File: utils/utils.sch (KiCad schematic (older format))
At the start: 37 parts, among them J1 AIN, J2 BIN, J3 GATE, J4 EURORACK_CONN_10, J5 ~OUT, J6 OUT, J7 Conn_01x04, J8 Conn_01x05, J9 Conn_01x03_Male, Q1 2N3904, U1 TL072, U2 4066, U3 LM317L_TO92, U4 LM337_SOT223

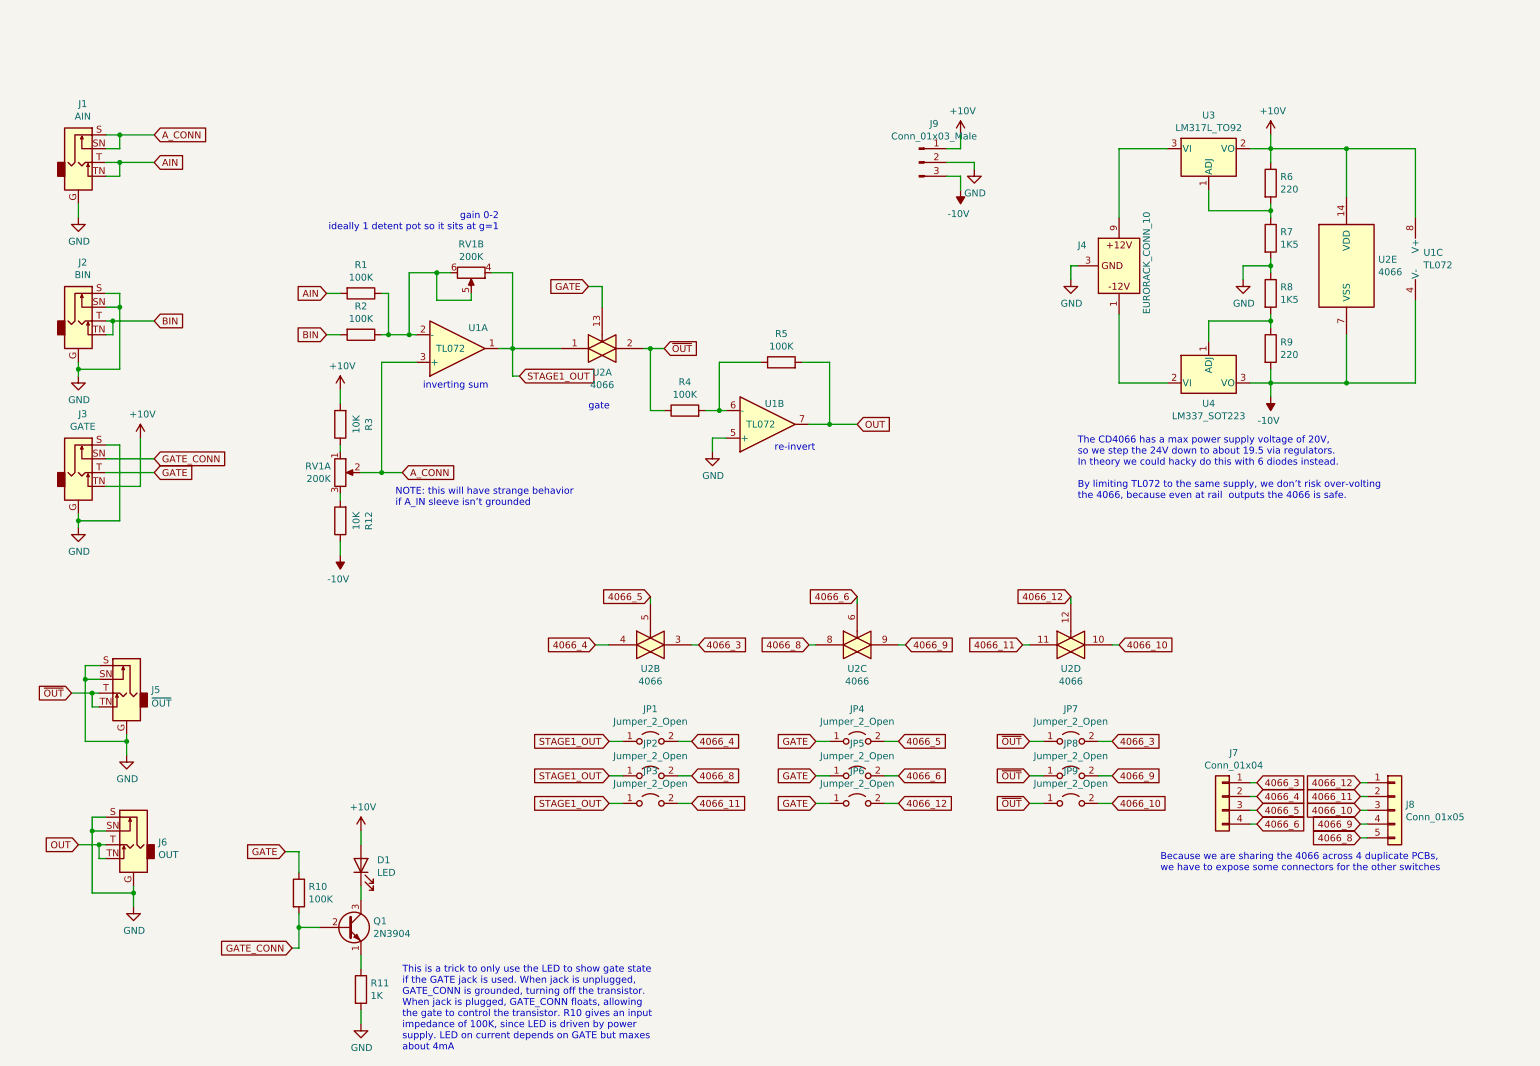
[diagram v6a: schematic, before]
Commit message: reworked utilities around better analog switch modules
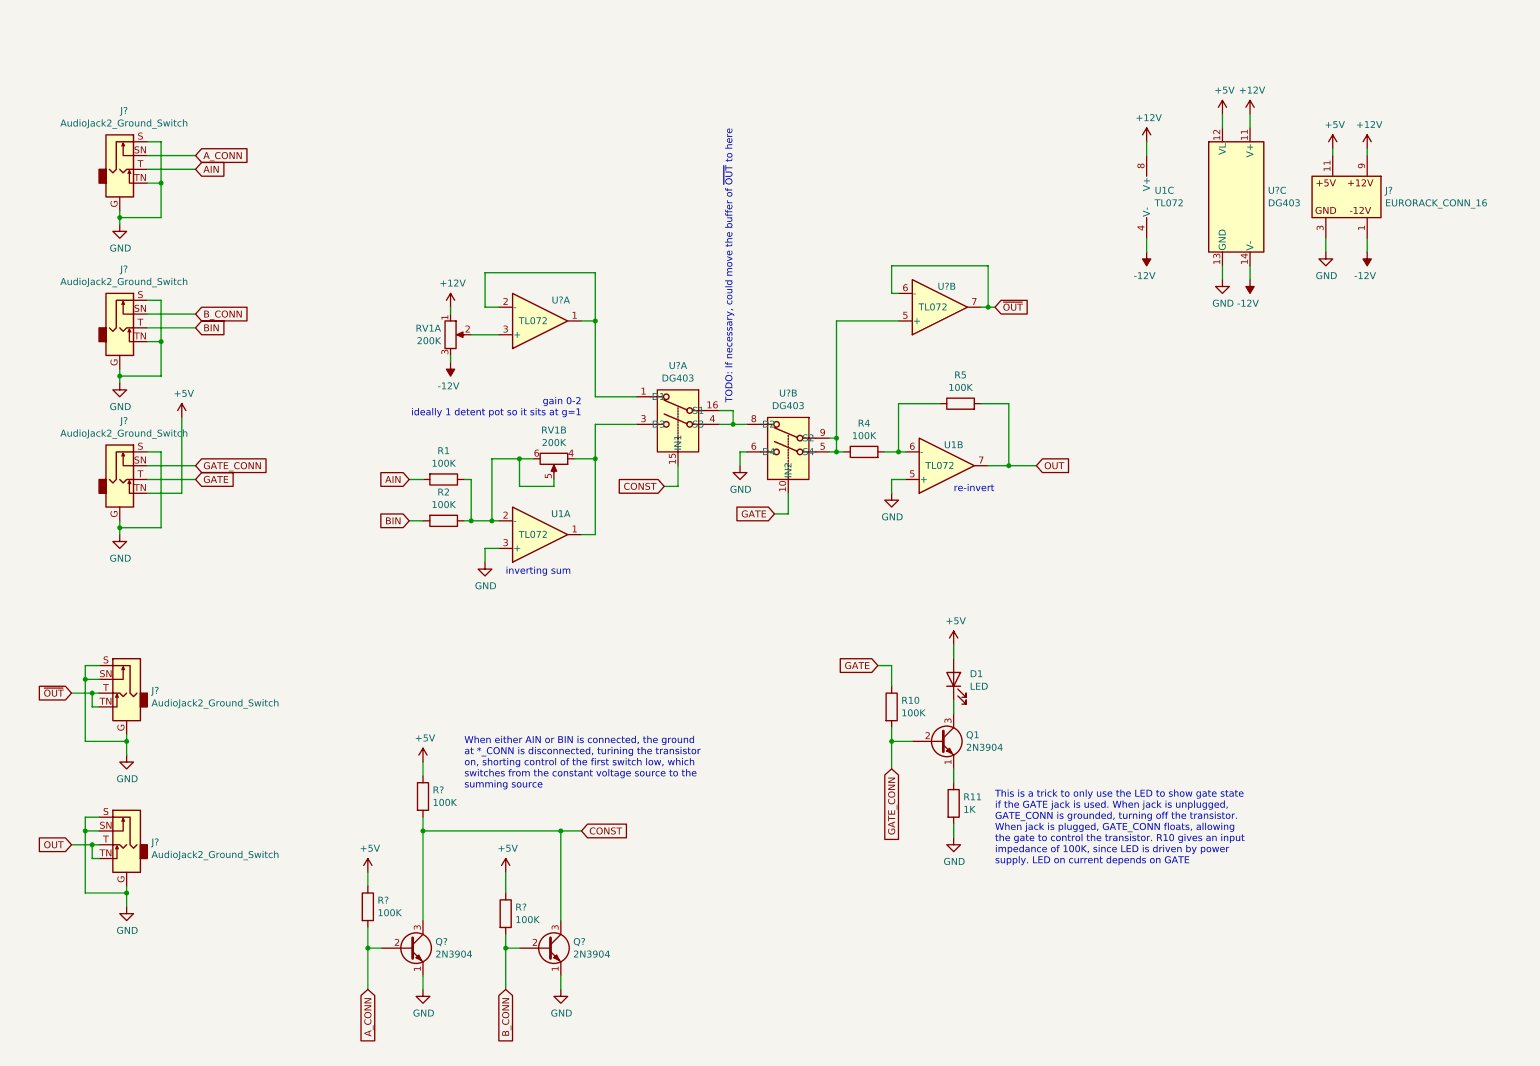
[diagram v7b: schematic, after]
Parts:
- removed J1: AIN, synth:Jack_3.5mm_Ledino_KB3SPRS_Horizontal, symbol synth:AudioJack2_Ground_Switch
- removed J2: BIN, synth:Jack_3.5mm_Ledino_KB3SPRS_Horizontal, symbol synth:AudioJack2_Ground_Switch
- removed J3: GATE, synth:Jack_3.5mm_Ledino_KB3SPRS_Horizontal, symbol synth:AudioJack2_Ground_Switch
- removed J4: EURORACK_CONN_10, synth:EURORACK_10_IDC, symbol synth:EURORACK_CONN_10
- removed J5: ~OUT, synth:Jack_3.5mm_Ledino_KB3SPRS_Horizontal, symbol synth:AudioJack2_Ground_Switch
- removed J6: OUT, synth:Jack_3.5mm_Ledino_KB3SPRS_Horizontal, symbol synth:AudioJack2_Ground_Switch
- removed J7: Conn_01x04, imciner2/KiCad-Libraries/modules/Connectors.pretty:CONN_2.54mm_1x05, symbol Connector_Generic:Conn_01x04
- removed J8: Conn_01x05, imciner2/KiCad-Libraries/modules/Connectors.pretty:CONN_2.54mm_1x05, symbol Connector_Generic:Conn_01x05
- removed J9: Conn_01x03_Male, 4ms/4ms-kicad-lib/4ms-footprints.pretty:Pin_Header_Straight_1x03, symbol Connector:Conn_01x03_Male
- removed JP1, JP2, JP3, JP4, JP5, JP6, JP7, JP8, JP9: Jumper_2_Open, fruchti/fruchtilib/mod/rcl.pretty:SOLDER_JUMPER_0603_B, symbol Jumper:Jumper_2_Open
- removed R12, R3: 10K, 4ms/4ms-kicad-lib/4ms-footprints.pretty:Resistor_TH_300, symbol Device:R
- removed R6, R9: 220, 4ms/4ms-kicad-lib/4ms-footprints.pretty:Resistor_TH_300, symbol Device:R
- removed R7, R8: 1K5, 4ms/4ms-kicad-lib/4ms-footprints.pretty:Resistor_TH_300, symbol Device:R
- removed U2: 4066, KiCad/kicad-footprints/Package_DIP.pretty:DIP-14_W7.62mm, symbol 4xxx:4066
- removed U3: LM317L_TO92, KiCad/TO_SOT_Packages_THT.pretty:TO-220-3_Vertical, symbol Regulator_Linear:LM317L_TO92
- removed U4: LM337_SOT223, KiCad/TO_SOT_Packages_THT.pretty:TO-220-3_Vertical, symbol Regulator_Linear:LM337_SOT223
- added J? (x5): AudioJack2_Ground_Switch, synth:3.5MM_Jack_Breakout_Vertical, symbol synth:AudioJack2_Ground_Switch
- added J?: EURORACK_CONN_16, synth:EURORACK_16_IDC, symbol synth:EURORACK_CONN_16
- added Q? (x2): 2N3904, 4ms/4ms-kicad-lib/lib-footprints/4ms_Package_TO.pretty:TO-92_OffsetPin2, symbol Transistor_BJT:2N3904
- added R? (x3): 100K, 4ms/4ms-kicad-lib/4ms-footprints.pretty:Resistor_TH_300, symbol Device:R
- added U? (x2): TL072, KiCad/kicad-footprints/Package_DIP.pretty:DIP-8_W7.62mm, symbol Amplifier_Operational:TL072
- added U? (x3): DG403, Package_SO:SOIC-16_3.9x9.9mm_P1.27mm, symbol synth:DG403
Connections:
- net -10V is gone; now on net -12V: U1.4 (V-)
- net AIN: now also J?.T
- net A_CONN: now also J?.SN, Q?.2 (B), R?.2; no longer RV1.2, U1.3 (+)
- net BIN: now also J?.T
- net GATE: now also J?.T, U?.10 (IN2)
- net GATE_CONN: now also J?.SN
- net GND: now also U1.3 (+), J?.3 (GND), J?.G, J?.G, J?.G, J?.G, J?.G, J?.S, J?.S, J?.S, J?.S, J?.S, J?.SN, J?.SN, J?.TN, J?.TN, Q?.1 (E), Q?.1 (E), U?.13 (GND), U?.6 (D4)
- net OUT: now also J?.T, J?.TN
- net ~OUT: now also J?.T, J?.TN, U?.6 (-), U?.7; no longer R4.1
- net +12V: now reaches RV1.1
- net +12V: now also U1.8 (V+), J?.9 (12V_P), U?.11 (V+)
- net -12V: now reaches RV1.3
- net -12V: now also J?.1 (12V_N), U?.14 (V-)
- net +10V renamed +5V
- net +5V: now also J?.11 (5V), J?.TN, R?.1, R?.1, R?.1, U?.12 (VL); no longer U1.8 (V+)
- net STAGE1_OUT: no longer names the net of RV1.4, U1.1
- net STAGE1_OUT: now also U?.3 (D3)
- new net: R4.1, U?.5 (+), U?.5 (S4), U?.9 (S2)
- new net: RV1.2, U?.3 (+)
- new net: U?.1, U?.1 (D1), U?.2 (-)
- new net: U?.16 (S1), U?.4 (S3), U?.8 (D2)
- new net B_CONN: J?.SN, Q?.2 (B), R?.2
- new net CONST: Q?.3 (C), Q?.3 (C), R?.2, U?.15 (IN1)
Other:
- note added: "TODO: If necessary, could move the buffer of ~OUT~ to here"
- note added: "This is a trick to only use the LED to show gate state\nif the GATE jack is used. When jack is unplugged,\nGATE_CONN is grounded, turning off the transistor.\nWhen jack is plugged, GATE_CONN floats, allowing\nthe gate to control the transistor. R10 gives an input\nimpedance of 100K, since LED is driven by power\nsupply. LED on current depends on GATE"
- note added: "When either AIN or BIN is connected, the ground\nat *_CONN is disconnected, turining the transistor\non, shorting control of the first switch low, which\nswitches from the constant voltage source to the\nsumming source"
- note removed: "Because we are sharing the 4066 across 4 duplicate PCBs,\nwe have to expose some connectors for the other switches"
- note removed: "NOTE: this will have strange behavior\nif A_IN sleeve isn’t grounded"
- note removed: "The CD4066 has a max power supply voltage of 20V,\nso we step the 24V down to about 19.5 via regulators.\nIn theory we could hacky do this with 6 diodes instead.\n\nBy limiting TL072 to the same supply, we don’t risk over-volting\nthe 4066, because even at rail outputs the 4066 is safe."
- note removed: "This is a trick to only use the LED to show gate state\nif the GATE jack is used. When jack is unplugged,\nGATE_CONN is grounded, turning off the transistor.\nWhen jack is plugged, GATE_CONN floats, allowing\nthe gate to control the transistor. R10 gives an input\nimpedance of 100K, since LED is driven by power\nsupply. LED on current depends on GATE but maxes\nabout 4mA"
- note removed: "gate"
- moved on the sheet: D1, Q1, R1, R10, R11, R2, R4, R5, RV1A, RV1B, U1A, U1B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

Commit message: restarted pcb
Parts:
- removed U1, U? (x2): TL072, KiCad/kicad-footprints/Package_DIP.pretty:DIP-8_W7.62mm, symbol Amplifier_Operational:TL072
- added U1: TL074, Package_DIP:DIP-14_W7.62mm, symbol Amplifier_Operational:TL074
- A_IN, B_IN, GATE1, OUT1, ~OUT1: renamed from J?; footprint synth:3.5MM_Jack_Breakout_Vertical -> synth:Jack_3.5mm_Ledino_KB3SPRS_Horizontal
- Q1, Q2: renamed from Q?; footprint 4ms/4ms-kicad-lib/lib-footprints/4ms_Package_TO.pretty:TO-92_OffsetPin2 -> Package_TO_SOT_THT:TO-92
- Q3: renamed from Q1; footprint 4ms/4ms-kicad-lib/lib-footprints/4ms_Package_TO.pretty:TO-92_OffsetPin2 -> Package_TO_SOT_THT:TO-92
- R1, R2, R5: renamed from R?; footprint 4ms/4ms-kicad-lib/4ms-footprints.pretty:Resistor_TH_300 -> Resistor_THT:R_Axial_DIN0309_L9.0mm_D3.2mm_P2.54mm_Vertical
- R3: renamed from R1; footprint 4ms/4ms-kicad-lib/4ms-footprints.pretty:Resistor_TH_300 -> Resistor_THT:R_Axial_DIN0309_L9.0mm_D3.2mm_P2.54mm_Vertical
- R4: renamed from R2; footprint 4ms/4ms-kicad-lib/4ms-footprints.pretty:Resistor_TH_300 -> Resistor_THT:R_Axial_DIN0309_L9.0mm_D3.2mm_P2.54mm_Vertical
- R6: renamed from R4; footprint 4ms/4ms-kicad-lib/4ms-footprints.pretty:Resistor_TH_300 -> Resistor_THT:R_Axial_DIN0309_L9.0mm_D3.2mm_P2.54mm_Vertical
- R7: renamed from R10; footprint 4ms/4ms-kicad-lib/4ms-footprints.pretty:Resistor_TH_300 -> Resistor_THT:R_Axial_DIN0309_L9.0mm_D3.2mm_P2.54mm_Vertical
- R8: renamed from R11; footprint 4ms/4ms-kicad-lib/4ms-footprints.pretty:Resistor_TH_300 -> Resistor_THT:R_Axial_DIN0309_L9.0mm_D3.2mm_P2.54mm_Vertical
- R9: renamed from R5; footprint 4ms/4ms-kicad-lib/4ms-footprints.pretty:Resistor_TH_300 -> Resistor_THT:R_Axial_DIN0309_L9.0mm_D3.2mm_P2.54mm_Vertical
- RV1: footprint 4ms/4ms-kicad-lib/4ms-footprints.pretty:Pin_Header_Straight_2x03_Pitch2.54mm -> Connector_PinHeader_2.54mm:PinHeader_2x03_P2.54mm_Vertical
- gave numbers to parts that had none: 2
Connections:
- net +12V: now also U1.4 (V+)
- net -12V: now also U1.11 (V-)
- net GND: now also U1.10 (+), U1.5 (+)
- net OUT: now also U1.8
- net ~OUT: now also U1.13 (-), U1.14
- net at R3.1, R4.1, RV1.5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: now also U1.6 (-)
- net at R6.1, U2.5 (S4), U2.9 (S2): now also U1.12 (+)
- net at R6.2, R9.1: now also U1.9 (-)
- net at RV1.4, U2.3 (D3): now also U1.7
- net at RV1.2: now also U1.3 (+)
- net at U2.1 (D1): now also U1.1, U1.2 (-)
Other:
- moved on the sheet: OUT1, ~{OUT1}
